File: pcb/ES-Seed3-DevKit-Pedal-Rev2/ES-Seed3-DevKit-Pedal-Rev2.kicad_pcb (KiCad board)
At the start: 2 copper layers, 197 x 100 mm, 151 parts, among them J1 DIN_MIDI_5P, J10 DIN_MIDI_5P, J11 DIN_MIDI_5P, J2 JACK_TRS_SWITCHING, J3 JACK_TRS_SWITCHING, J4 JACK_TRS_SWITCHING, J5 JACK_TRS_SWITCHING, J6 JACK_TRS_SWITCHING, J7 USB4110GFA, J8 Barrel_Jack_Switch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

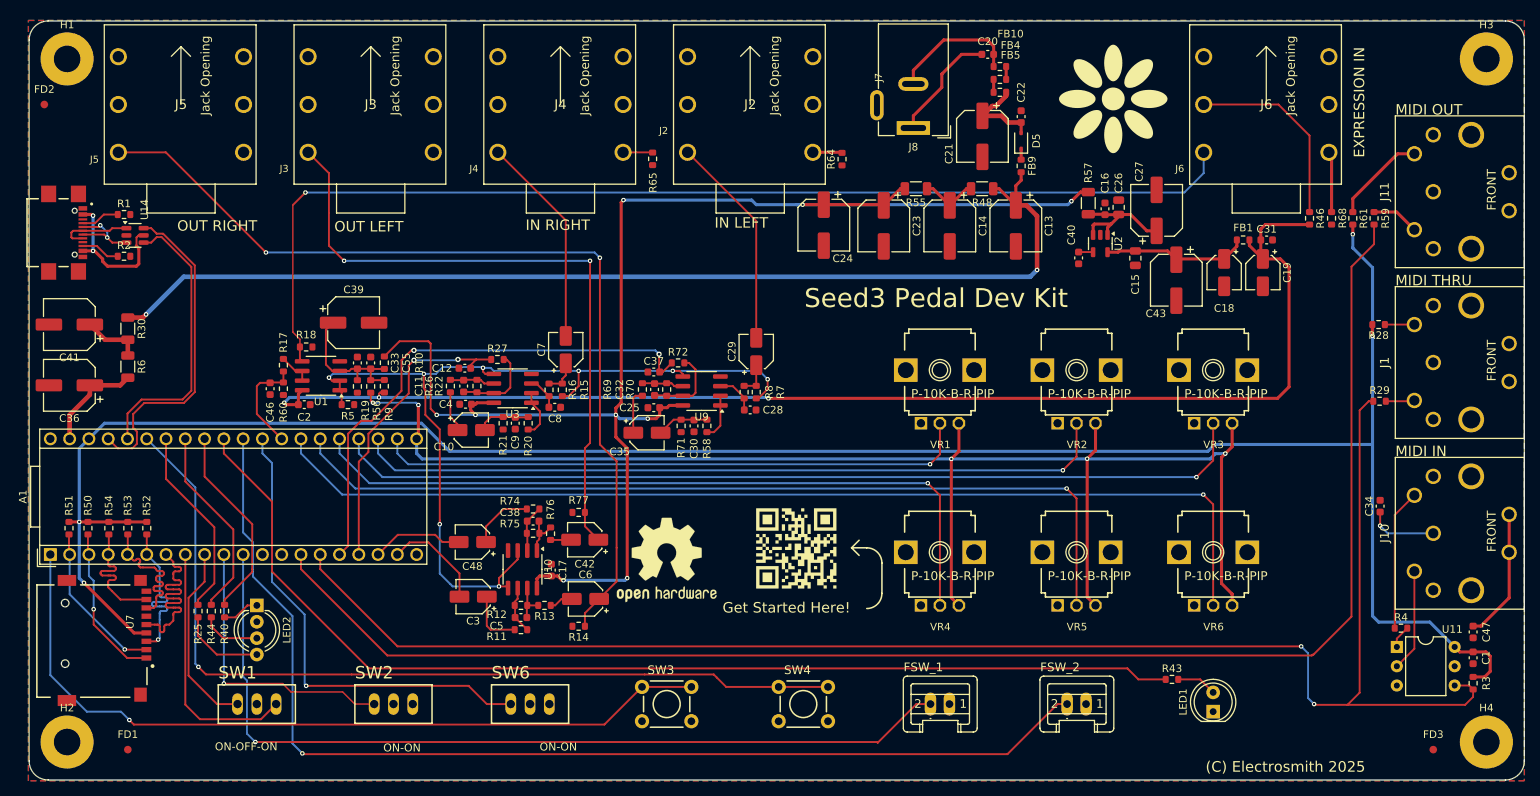
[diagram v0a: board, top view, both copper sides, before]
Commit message: more silk fixes, and removed paste from toggles
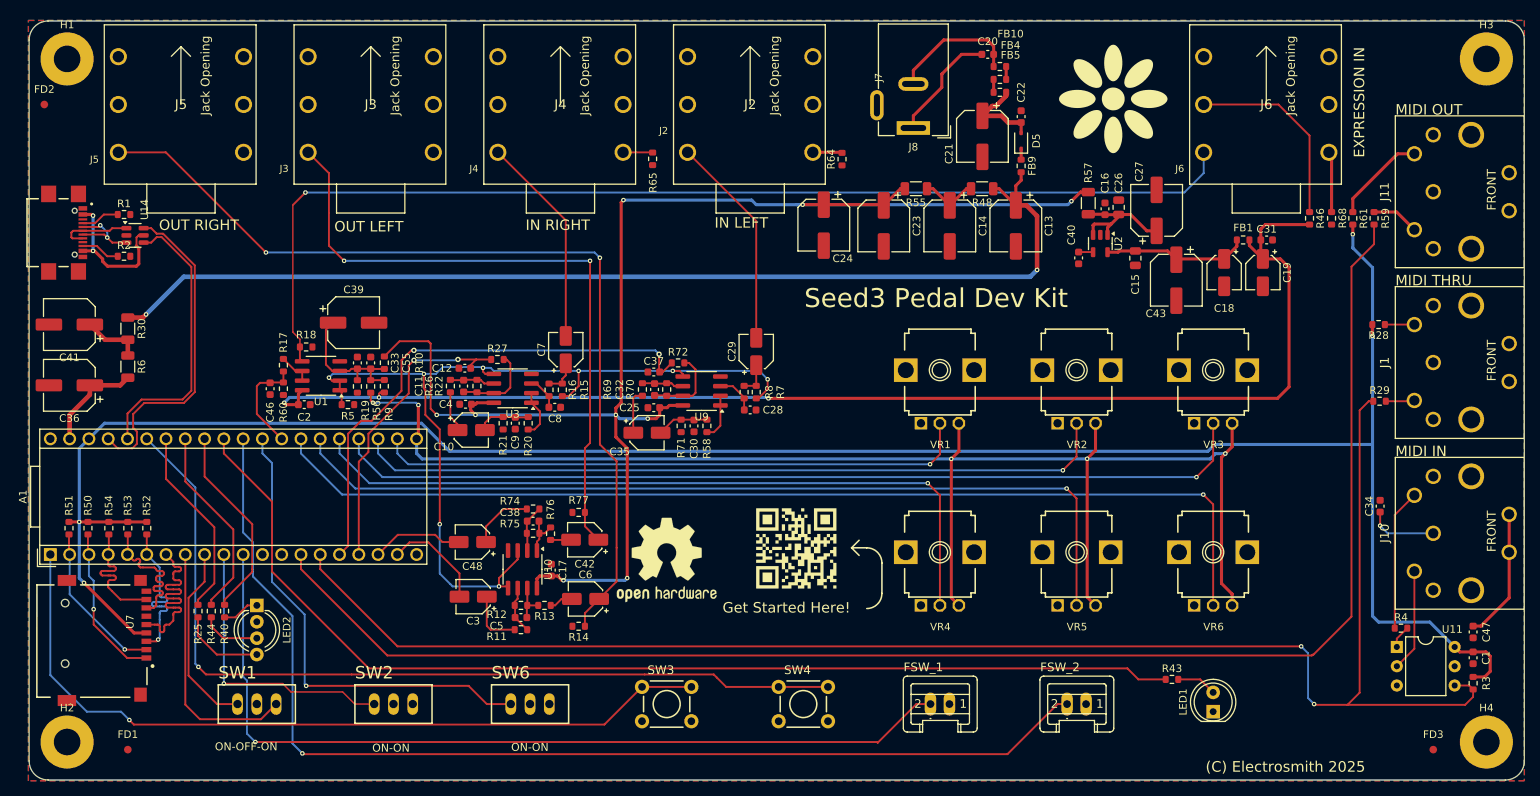
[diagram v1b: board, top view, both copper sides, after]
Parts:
- SW1, SW2, SW6: footprint parts-for-kicad:TOGGLE_SILK_PIP -> parts-for-kicad:TOGGLE_ON_OFF_ON
